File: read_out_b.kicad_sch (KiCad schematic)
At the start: 26 parts, among them J2 Bus_PCI_Express_x16, U19 74LS541, U20 74LS541, U21 74LS541, U22 74LS541, U23 74LS541, U24 74LS541, U25 74LS541, U26 74LS541, U27 74LS04, U28 74LS30

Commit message: Current progress.  Working on laying out the latched bus.
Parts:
- C22: renamed from C19; footprint (none) -> Capacitor_SMD:C_0805_2012Metric_Pad1.18x1.45mm_HandSolder
- C23: renamed from C20; footprint (none) -> Capacitor_SMD:C_0805_2012Metric_Pad1.18x1.45mm_HandSolder
- C24: renamed from C21; footprint (none) -> Capacitor_SMD:C_0805_2012Metric_Pad1.18x1.45mm_HandSolder
- C25: renamed from C22; footprint (none) -> Capacitor_SMD:C_0805_2012Metric_Pad1.18x1.45mm_HandSolder
- C26: renamed from C23; footprint (none) -> Capacitor_SMD:C_0805_2012Metric_Pad1.18x1.45mm_HandSolder
- C27: renamed from C24; footprint (none) -> Capacitor_SMD:C_0805_2012Metric_Pad1.18x1.45mm_HandSolder
- C28: renamed from C25; footprint (none) -> Capacitor_SMD:C_0805_2012Metric_Pad1.18x1.45mm_HandSolder
- C29: renamed from C26; footprint (none) -> Capacitor_SMD:C_0805_2012Metric_Pad1.18x1.45mm_HandSolder
- C30: renamed from C27; footprint (none) -> Capacitor_SMD:C_0805_2012Metric_Pad1.18x1.45mm_HandSolder
- C31: renamed from C28; footprint (none) -> Capacitor_SMD:C_0805_2012Metric_Pad1.18x1.45mm_HandSolder
- JP11: renamed from JP6; footprint (none) -> Jumper:SolderJumper-3_P1.3mm_Open_RoundedPad1.0x1.5mm
- JP12: renamed from JP7; footprint (none) -> Jumper:SolderJumper-3_P1.3mm_Open_RoundedPad1.0x1.5mm
- JP13: renamed from JP8; footprint (none) -> Jumper:SolderJumper-3_P1.3mm_Open_RoundedPad1.0x1.5mm
- JP14: renamed from JP9; footprint (none) -> Jumper:SolderJumper-3_P1.3mm_Open_RoundedPad1.0x1.5mm
- JP15: renamed from JP10; footprint (none) -> Jumper:SolderJumper-3_P1.3mm_Open_RoundedPad1.0x1.5mm
- U22: renamed from U19; footprint (none) -> Package_SO:SOIC-20W_7.5x12.8mm_P1.27mm
- U23: renamed from U20; footprint (none) -> Package_SO:SOIC-20W_7.5x12.8mm_P1.27mm
- U24: renamed from U21; footprint (none) -> Package_SO:SOIC-20W_7.5x12.8mm_P1.27mm
- U25: renamed from U22; footprint (none) -> Package_SO:SOIC-20W_7.5x12.8mm_P1.27mm
- U26: renamed from U23; footprint (none) -> Package_SO:SOIC-20W_7.5x12.8mm_P1.27mm
- U27: renamed from U24; footprint (none) -> Package_SO:SOIC-20W_7.5x12.8mm_P1.27mm
- U28: renamed from U25; footprint (none) -> Package_SO:SOIC-20W_7.5x12.8mm_P1.27mm
- U29: renamed from U26; footprint (none) -> Package_SO:SOIC-20W_7.5x12.8mm_P1.27mm
- U30: renamed from U27; footprint (none) -> Package_SO:SOIC-14_3.9x8.7mm_P1.27mm
- U31: renamed from U28; footprint (none) -> Package_SO:SOIC-14_3.9x8.7mm_P1.27mm
- renumbered J2 to J3
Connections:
- net ~{read_b_en}: now also U25.1 (G1)
- net CLK_PH0: no longer names the net of J3.A13 (REFCLK+)
- net CLK_PH1: no longer names the net of J3.A14 (REFCLK-)
- net latched00 renamed latched0
- net latched01 renamed latched1
- net latched02 renamed latched2
- net latched03 renamed latched3
- net latched04 renamed latched4
- net latched05 renamed latched5
- net latched06 renamed latched6
- net latched07 renamed latched7
- net latched08 renamed latched8
- net latched09 renamed latched9
- net read_b00 renamed read_b0
- net read_b01 renamed read_b1
- net read_b02 renamed read_b2
- net read_b03 renamed read_b3
- net read_b04 renamed read_b4
- net read_b05 renamed read_b5
- net read_b06 renamed read_b6
- net read_b07 renamed read_b7
- net read_b08 renamed read_b8
- net read_b09 renamed read_b9
- net ~{RST}: no longer names the net of J3.A11 (~{PERST})
- no-connect marks 17 -> 20

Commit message: Progress on Read B Port.
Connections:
- net latched0: now also U22.9 (A7); no longer U22.2 (A0)
- net latched1: now also U22.8 (A6); no longer U22.3 (A1)
- net latched10: now also U23.7 (A5); no longer U23.4 (A2)
- net latched11: now also U23.6 (A4); no longer U23.5 (A3)
- net latched12: now also U23.5 (A3); no longer U23.6 (A4)
- net latched13: now also U23.4 (A2); no longer U23.7 (A5)
- net latched14: now also U23.3 (A1); no longer U23.8 (A6)
- net latched15: now also U23.2 (A0); no longer U23.9 (A7)
- net latched16: now also U24.9 (A7); no longer U24.2 (A0)
- net latched17: now also U24.8 (A6); no longer U24.3 (A1)
- net latched18: now also U24.7 (A5); no longer U24.4 (A2)
- net latched19: now also U24.6 (A4); no longer U24.5 (A3)
- net latched2: now also U22.7 (A5); no longer U22.4 (A2)
- net latched20: now also U24.5 (A3); no longer U24.6 (A4)
- net latched21: now also U24.4 (A2); no longer U24.7 (A5)
- net latched22: now also U24.3 (A1); no longer U24.8 (A6)
- net latched23: now also U24.2 (A0); no longer U24.9 (A7)
- net latched24: now also U25.9 (A7); no longer U25.2 (A0)
- net latched25: now also U25.8 (A6); no longer U25.3 (A1)
- net latched26: now also U25.7 (A5); no longer U25.4 (A2)
- net latched27: now also U25.6 (A4); no longer U25.5 (A3)
- net latched28: now also U25.5 (A3); no longer U25.6 (A4)
- net latched29: now also U25.4 (A2); no longer U25.7 (A5)
- net latched3: now also U22.6 (A4); no longer U22.5 (A3)
- net latched30: now also U25.3 (A1); no longer U25.8 (A6)
- net latched31: now also U25.2 (A0); no longer U25.9 (A7)
- net latched4: now also U22.5 (A3); no longer U22.6 (A4)
- net latched5: now also U22.4 (A2); no longer U22.7 (A5)
- net latched6: now also U22.3 (A1); no longer U22.8 (A6)
- net latched7: now also U22.2 (A0); no longer U22.9 (A7)
- net latched8: now also U23.9 (A7); no longer U23.2 (A0)
- net latched9: now also U23.8 (A6); no longer U23.3 (A1)
- net read_b0: now also U22.11 (Y7); no longer U22.18 (Y0)
- net read_b1: now also U22.12 (Y6); no longer U22.17 (Y1)
- net read_b10: now also U23.13 (Y5); no longer U23.16 (Y2)
- net read_b11: now also U23.14 (Y4); no longer U23.15 (Y3)
- net read_b12: now also U23.15 (Y3); no longer U23.14 (Y4)
- net read_b13: now also U23.16 (Y2); no longer U23.13 (Y5)
- net read_b14: now also U23.17 (Y1); no longer U23.12 (Y6)
- net read_b15: now also U23.18 (Y0); no longer U23.11 (Y7)
- net read_b16: now also U24.11 (Y7); no longer U24.18 (Y0)
- net read_b17: now also U24.12 (Y6); no longer U24.17 (Y1)
- net read_b18: now also U24.13 (Y5); no longer U24.16 (Y2)
- net read_b19: now also U24.14 (Y4); no longer U24.15 (Y3)
- net read_b2: now also U22.13 (Y5); no longer U22.16 (Y2)
- net read_b20: now also U24.15 (Y3); no longer U24.14 (Y4)
- net read_b21: now also U24.16 (Y2); no longer U24.13 (Y5)
- net read_b22: now also U24.17 (Y1); no longer U24.12 (Y6)
- net read_b23: now also U24.18 (Y0); no longer U24.11 (Y7)
- net read_b24: now also U25.11 (Y7); no longer U25.18 (Y0)
- net read_b25: now also U25.12 (Y6); no longer U25.17 (Y1)
- net read_b26: now also U25.13 (Y5); no longer U25.16 (Y2)
- net read_b27: now also U25.14 (Y4); no longer U25.15 (Y3)
- net read_b28: now also U25.15 (Y3); no longer U25.14 (Y4)
- net read_b29: now also U25.16 (Y2); no longer U25.13 (Y5)
- net read_b3: now also U22.14 (Y4); no longer U22.15 (Y3)
- net read_b30: now also U25.17 (Y1); no longer U25.12 (Y6)
- net read_b31: now also U25.18 (Y0); no longer U25.11 (Y7)
- net read_b4: now also U22.15 (Y3); no longer U22.14 (Y4)
- net read_b5: now also U22.16 (Y2); no longer U22.13 (Y5)
- net read_b6: now also U22.17 (Y1); no longer U22.12 (Y6)
- net read_b7: now also U22.18 (Y0); no longer U22.11 (Y7)
- net read_b8: now also U23.11 (Y7); no longer U23.18 (Y0)
- net read_b9: now also U23.12 (Y6); no longer U23.17 (Y1)
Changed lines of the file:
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@@
 	)
 	(label "latched4"
-		(at 72.39 49.53 180)
+		(at 72.39 46.99 180)
 		(effects
 			(font
@@
 	)
 	(label "latched15"
-		(at 72.39 111.76 180)
+		(at 72.39 93.98 180)
 		(effects
 			(font
@@
 	)
 	(label "latched16"
-		(at 72.39 148.59 180)
+		(at 72.39 166.37 180)
 		(effects
 			(font
@@
 	)
 	(label "read_b13"
-		(at 97.79 106.68 0)
+		(at 97.79 99.06 0)
 		(effects
 			(font
@@
 	)
 	(label "read_b17"
-		(at 97.79 151.13 0)
+		(at 97.79 163.83 0)
 		(effects
 			(font
@@
 	)
 	(label "latched3"
-		(at 72.39 46.99 180)
+		(at 72.39 49.53 180)
 		(effects
 			(font
@@
 	)
 	(label "read_b12"
-		(at 97.79 104.14 0)
+		(at 97.79 101.6 0)
 		(effects
 			(font
@@
 	)
 	(label "read_b1"
-		(at 97.79 41.91 0)
+		(at 97.79 54.61 0)
 		(effects
 			(font
@@
 	)
 	(label "read_b0"
-		(at 97.79 39.37 0)
+		(at 97.79 57.15 0)
 		(effects
 			(font
@@
 	)
 	(label "read_b24"
-		(at 97.79 203.2 0)
+		(at 97.79 220.98 0)
 		(effects
 			(font
@@
 	)
 	(label "read_b16"
-		(at 97.79 148.59 0)
+		(at 97.79 166.37 0)
 		(effects
 			(font
@@
 	)
 	(label "read_b11"
-		(at 97.79 101.6 0)
+		(at 97.79 104.14 0)
 		(effects
 			(font
@@
 	)
 	(label "read_b19"
-		(at 97.79 156.21 0)
+		(at 97.79 158.75 0)
 		(effects
 			(font
@@
 	)
 	(label "read_b26"
-		(at 97.79 208.28 0)
+		(at 97.79 215.9 0)
 		(effects
 			(font
@@
 	)
 	(label "latched2"
-		(at 72.39 44.45 180)
+		(at 72.39 52.07 180)
 		(effects
 			(font
@@
 	)
 	(label "latched29"
-		(at 72.39 215.9 180)
+		(at 72.39 208.28 180)
 		(effects
 			(font
@@
 	)
 	(label "latched25"
-		(at 72.39 205.74 180)
+		(at 72.39 218.44 180)
 		(effects
 			(font
@@
 	)
 	(label "latched9"
-		(at 72.39 96.52 180)
+		(at 72.39 109.22 180)
 		(effects
 			(font
@@
 	)
 	(label "latched11"
-		(at 72.39 101.6 180)
+		(at 72.39 104.14 180)
 		(effects
 			(font
@@
 	)
 	(label "latched17"
-		(at 72.39 151.13 180)
+		(at 72.39 163.83 180)
 		(effects
 			(font
@@
 	)
 	(label "latched30"
-		(at 72.39 218.44 180)
+		(at 72.39 205.74 180)
 		(effects
 			(font
@@
 	)
 	(label "read_b15"
-		(at 97.79 111.76 0)
+		(at 97.79 93.98 0)
 		(effects
 			(font
@@
 	)
 	(label "read_b2"
-		(at 97.79 44.45 0)
+		(at 97.79 52.07 0)
 		(effects
 			(font
@@
 	)
 	(label "read_b9"
-		(at 97.79 96.52 0)
+		(at 97.79 109.22 0)
 		(effects
 			(font
@@
 	)
 	(label "latched12"
-		(at 72.39 104.14 180)
+		(at 72.39 101.6 180)
 		(effects
 			(font
@@
 	)
 	(label "latched14"
-		(at 72.39 109.22 180)
+		(at 72.39 96.52 180)
 		(effects
 			(font
@@
 	)
 	(label "latched28"
-		(at 72.39 213.36 180)
+		(at 72.39 210.82 180)
 		(effects
 			(font
@@
 	)
 	(label "read_b27"
-		(at 97.79 210.82 0)
+		(at 97.79 213.36 0)
 		(effects
 			(font
@@
 	)
 	(label "read_b6"
-		(at 97.79 54.61 0)
+		(at 97.79 41.91 0)
 		(effects
 			(font
@@
 	)
 	(label "read_b28"
-		(at 97.79 213.36 0)
+		(at 97.79 210.82 0)
 		(effects
 			(font
@@
 	)
 	(label "read_b29"
-		(at 97.79 215.9 0)
+		(at 97.79 208.28 0)
 		(effects
 			(font
@@
 	)
 	(label "latched19"
-		(at 72.39 156.21 180)
+		(at 72.39 158.75 180)
 		(effects
 			(font
@@
 	)
 	(label "latched0"
-		(at 72.39 39.37 180)
+		(at 72.39 57.15 180)
 		(effects
 			(font
@@
 	)
 	(label "read_b10"
-		(at 97.79 99.06 0)
+		(at 97.79 106.68 0)
 		(effects
 			(font
@@
 	)
 	(label "latched1"
-		(at 72.39 41.91 180)
+		(at 72.39 54.61 180)
 		(effects
 			(font
@@
 	)
 	(label "latched7"
-		(at 72.39 57.15 180)
+		(at 72.39 39.37 180)
 		(effects
 			(font
@@
 	)
 	(label "read_b4"
-		(at 97.79 49.53 0)
+		(at 97.79 46.99 0)
 		(effects
 			(font
@@
 	)
 	(label "latched26"
-		(at 72.39 208.28 180)
+		(at 72.39 215.9 180)
 		(effects
 			(font
@@
 	)
 	(label "latched5"
-		(at 72.39 52.07 180)
+		(at 72.39 44.45 180)
 		(effects
 			(font
@@
 	)
 	(label "latched10"
-		(at 72.39 99.06 180)
+		(at 72.39 106.68 180)
 		(effects
 			(font
@@
 	)
 	(label "read_b7"
-		(at 97.79 57.15 0)
+		(at 97.79 39.37 0)
 		(effects
 			(font
@@
 	)
 	(label "read_b18"
-		(at 97.79 153.67 0)
+		(at 97.79 161.29 0)
 		(effects
 			(font
@@
 	)
 	(label "latched13"
-		(at 72.39 106.68 180)
+		(at 72.39 99.06 180)
 		(effects
 			(font
@@
 	)
 	(label "latched27"
-		(at 72.39 210.82 180)
+		(at 72.39 213.36 180)
 		(effects
 			(font
@@
 	)
 	(label "latched18"
-		(at 72.39 153.67 180)
+		(at 72.39 161.29 180)
 		(effects
 			(font
@@
 	)
 	(label "read_b14"
-		(at 97.79 109.22 0)
+		(at 97.79 96.52 0)
 		(effects
 			(font
@@
 	)
 	(label "latched20"
-		(at 72.39 158.75 180)
+		(at 72.39 156.21 180)
 		(effects
 			(font
@@
 	)
 	(label "read_b23"
-		(at 97.79 166.37 0)
+		(at 97.79 148.59 0)
 		(effects
 			(font
@@
 	)
 	(label "read_b30"
-		(at 97.79 218.44 0)
+		(at 97.79 205.74 0)
 		(effects
 			(font
@@
 	)
 	(label "latched23"
-		(at 72.39 166.37 180)
+		(at 72.39 148.59 180)
 		(effects
 			(font
@@
 	)
 	(label "read_b3"
-		(at 97.79 46.99 0)
+		(at 97.79 49.53 0)
 		(effects
 			(font
@@
 	)
 	(label "read_b21"
-		(at 97.79 161.29 0)
+		(at 97.79 153.67 0)
 		(effects
 			(font
@@
 	)
 	(label "latched6"
-		(at 72.39 54.61 180)
+		(at 72.39 41.91 180)
 		(effects
 			(font
@@
 	)
 	(label "read_b8"
-		(at 97.79 93.98 0)
+		(at 97.79 111.76 0)
 		(effects
 			(font
@@
 	)
 	(label "read_b5"
-		(at 97.79 52.07 0)
+		(at 97.79 44.45 0)
 		(effects
 			(font
@@
 	)
 	(label "latched22"
-		(at 72.39 163.83 180)
+		(at 72.39 151.13 180)
 		(effects
 			(font
@@
 	)
 	(label "latched8"
-		(at 72.39 93.98 180)
+		(at 72.39 111.76 180)
 		(effects
 			(font
@@
 	)
 	(label "read_b22"
-		(at 97.79 163.83 0)
+		(at 97.79 151.13 0)
 		(effects
 			(font
@@
 	)
 	(label "latched31"
-		(at 72.39 220.98 180)
+		(at 72.39 203.2 180)
 		(effects
 			(font
@@
 	)
 	(label "read_b20"
-		(at 97.79 158.75 0)
+		(at 97.79 156.21 0)
 		(effects
 			(font
@@
 	)
 	(label "latched21"
-		(at 72.39 161.29 180)
+		(at 72.39 153.67 180)
 		(effects
 			(font
@@
 	)
 	(label "read_b25"
-		(at 97.79 205.74 0)
+		(at 97.79 218.44 0)
 		(effects
 			(font
@@
 	)
 	(label "latched24"
-		(at 72.39 203.2 180)
+		(at 72.39 220.98 180)
 		(effects
 			(font
@@
 	)
 	(label "read_b31"
-		(at 97.79 220.98 0)
-		(effects
-			(font
+		(at 97.79 203.2 0)
+		(effects
+			(font

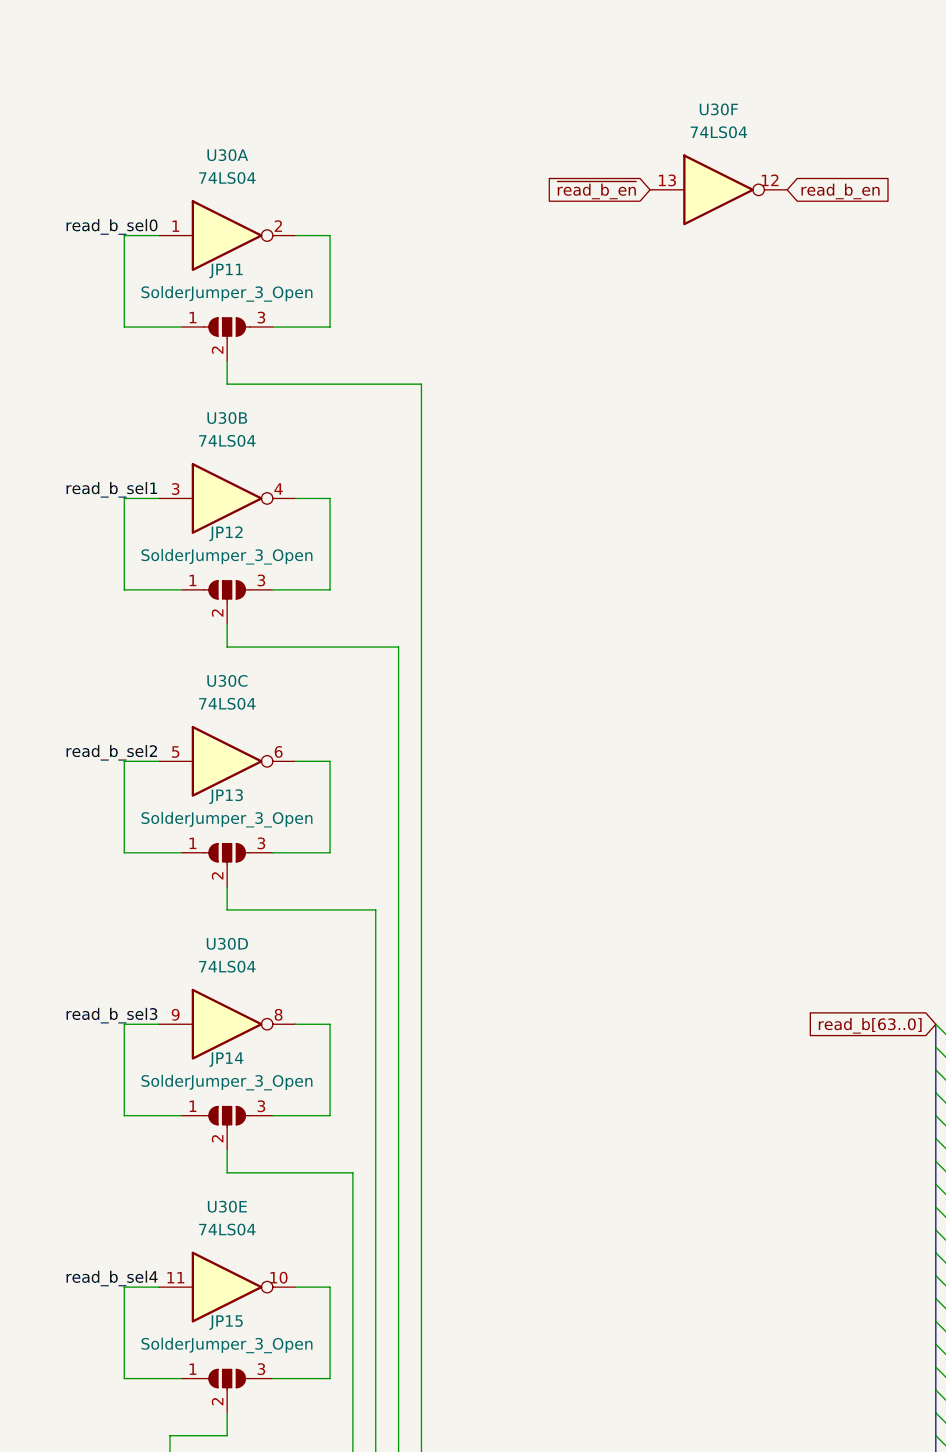
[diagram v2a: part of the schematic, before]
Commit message: Finished the register board layout.  It's not as short as I would have liked, but it's done.  64 bit busses take an amount of space.
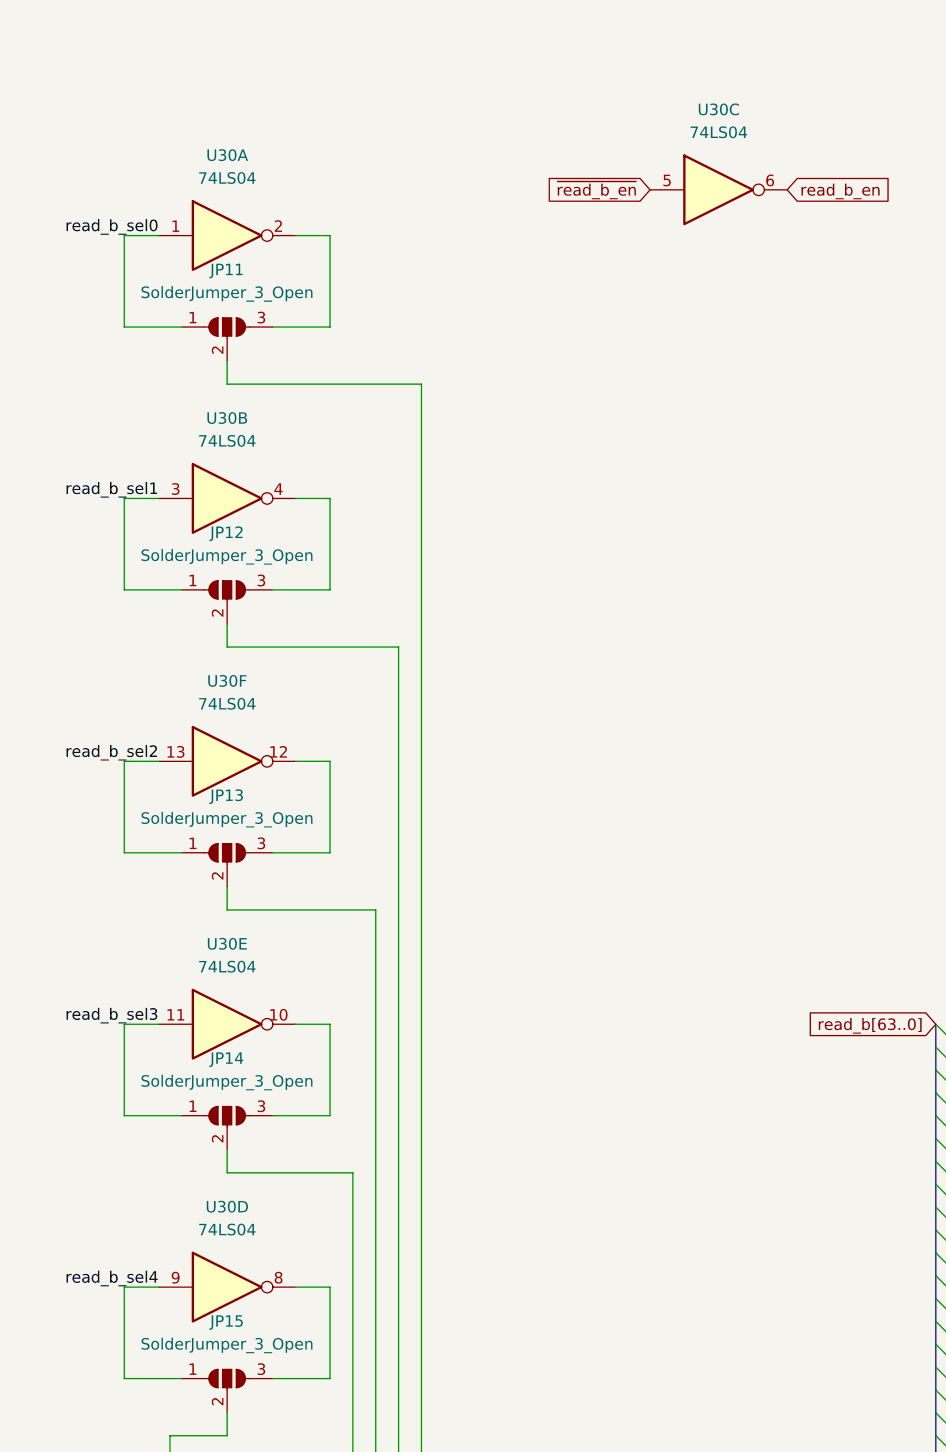
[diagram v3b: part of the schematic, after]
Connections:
- net read_b_en: now also U30.6; no longer U30.12
- net read_b_sel2: now also U30.13; no longer U30.5
- net read_b_sel3: now also U30.11; no longer U30.9
- net read_b_sel4: now also U30.9; no longer U30.11
- net ~{read_b_en}: now also U30.5; no longer U30.13
- net at U30.8: now also JP15.3 (B); no longer JP14.3 (B)
- net at U30.10: now also JP14.3 (B); no longer JP15.3 (B)
- net at JP13.3 (B): now also U30.12; no longer U30.6
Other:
- moved on the sheet: U30C, U30D, U30E, U30F
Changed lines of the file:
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@@
 	(symbol
 		(lib_id "74xx:74LS04")
-		(at 318.77 38.1 0)
+		(at 264.16 101.6 0)
 		(unit 6)
 		(exclude_from_sim no)
@@
 		(fields_autoplaced yes)
 		(property "Reference" "U30"
-			(at 318.77 29.21 0)
+			(at 264.16 92.71 0)
 			(effects
 				(font
@@
 		)
 		(property "Value" "74LS04"
-			(at 318.77 31.75 0)
+			(at 264.16 95.25 0)
 			(effects
 				(font
@@
 		)
 		(property "Footprint" "Package_SO:SOIC-14_3.9x8.7mm_P1.27mm"
-			(at 318.77 38.1 0)
+			(at 264.16 101.6 0)
 			(effects
 				(font
@@
 		)
 		(property "Datasheet" "http://www.ti.com/lit/gpn/sn74LS04"
-			(at 318.77 38.1 0)
+			(at 264.16 101.6 0)
 			(effects
 				(font
@@
 		)
 		(property "Description" "Hex Inverter"
-			(at 318.77 38.1 0)
+			(at 264.16 101.6 0)
 			(effects
 				(font
@@
 	(symbol
 		(lib_id "74xx:74LS04")
-		(at 264.16 130.81 0)
+		(at 264.16 160.02 0)
 		(unit 4)
 		(exclude_from_sim no)
@@
 		(fields_autoplaced yes)
 		(property "Reference" "U30"
-			(at 264.16 121.92 0)
+			(at 264.16 151.13 0)
 			(effects
 				(font
@@
 		)
 		(property "Value" "74LS04"
-			(at 264.16 124.46 0)
+			(at 264.16 153.67 0)
 			(effects
 				(font
@@
 		)
 		(property "Footprint" "Package_SO:SOIC-14_3.9x8.7mm_P1.27mm"
-			(at 264.16 130.81 0)
+			(at 264.16 160.02 0)
 			(effects
 				(font
@@
 		)
 		(property "Datasheet" "http://www.ti.com/lit/gpn/sn74LS04"
-			(at 264.16 130.81 0)
+			(at 264.16 160.02 0)
 			(effects
 				(font
@@
 		)
 		(property "Description" "Hex Inverter"
-			(at 264.16 130.81 0)
+			(at 264.16 160.02 0)
 			(effects
 				(font
@@
 	(symbol
 		(lib_id "74xx:74LS04")
-		(at 264.16 160.02 0)
+		(at 264.16 130.81 0)
 		(unit 5)
 		(exclude_from_sim no)
@@
 		(fields_autoplaced yes)
 		(property "Reference" "U30"
-			(at 264.16 151.13 0)
+			(at 264.16 121.92 0)
 			(effects
 				(font
@@
 		)
 		(property "Value" "74LS04"
-			(at 264.16 153.67 0)
+			(at 264.16 124.46 0)
 			(effects
 				(font
@@
 		)
 		(property "Footprint" "Package_SO:SOIC-14_3.9x8.7mm_P1.27mm"
-			(at 264.16 160.02 0)
+			(at 264.16 130.81 0)
 			(effects
 				(font
@@
 		)
 		(property "Datasheet" "http://www.ti.com/lit/gpn/sn74LS04"
-			(at 264.16 160.02 0)
+			(at 264.16 130.81 0)
 			(effects
 				(font
@@
 		)
 		(property "Description" "Hex Inverter"
-			(at 264.16 160.02 0)
+			(at 264.16 130.81 0)
 			(effects
 				(font
@@
 	(symbol
 		(lib_id "74xx:74LS04")
-		(at 264.16 101.6 0)
+		(at 318.77 38.1 0)
 		(unit 3)
 		(exclude_from_sim no)
@@
 		(fields_autoplaced yes)
 		(property "Reference" "U30"
-			(at 264.16 92.71 0)
+			(at 318.77 29.21 0)
 			(effects
 				(font
@@
 		)
 		(property "Value" "74LS04"
-			(at 264.16 95.25 0)
+			(at 318.77 31.75 0)
 			(effects
 				(font
@@
 		)
 		(property "Footprint" "Package_SO:SOIC-14_3.9x8.7mm_P1.27mm"
-			(at 264.16 101.6 0)
+			(at 318.77 38.1 0)
 			(effects
 				(font
@@
 		)
 		(property "Datasheet" "http://www.ti.com/lit/gpn/sn74LS04"
-			(at 264.16 101.6 0)
+			(at 318.77 38.1 0)
 			(effects
 				(font
@@
 		)
 		(property "Description" "Hex Inverter"
-			(at 264.16 101.6 0)
+			(at 318.77 38.1 0)
 			(effects
 				(font
